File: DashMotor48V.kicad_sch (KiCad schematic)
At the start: 27 parts, among them U1 TPS629203DRLR, U2 TPS629203DRLR, U3 DRV8353SRTAR

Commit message: include the mosfet
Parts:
- added C13: 100nF 50V, dash:CC0603JRX7R9BB104, symbol dash:CC0603JRX7R9BB104
- added C14: GRM155R60J475ME87D, dash:GRM155R60J475ME87D, symbol dash:GRM155R60J475ME87D
- added C15, C16, C17, C18, C19, C20, C21, C22, C23, C24, C25, C26, C27, C28, C29, C30: 10uF, dash:GRM32EC72A106KE05L, symbol dash:GRM32EC72A106KE05L
- added FL1: choe, dash:BLM18AG601SN1D, symbol dash:BLM18AG601SN1D
- added H1, H2, H3: MountingHole_Pad, symbol Mechanical:MountingHole_Pad
- added Q1, Q2, Q3, Q4, Q5, Q6: FDMS039N08B, dash:FDMS039N08B, symbol dash:FDMS039N08B
- added R10: 10K, dash:RT0402DRE0710KL, symbol dash:RT0402DRE0710KL
- added R11, R12: WSLF25121L000FEA, dash:WSLF25121L000FEA, symbol dash:WSLF25121L000FEA
- added R9: 150K 1%, dash:RC0402FR_07150KL, symbol dash:RC0402FR_07150KL
- added U4: STM32F446RCT6, dash:STM32F446RCT6, symbol dash:STM32F446RCT6
- added Y1: CSTNE8M00G550000R0, dash:CSTNE8M00G550000R0, symbol dash:CSTNE8M00G550000R0
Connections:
- net +3.3V: now also FL1.1, U4.1 (VBAT), U4.19 (VDD_4), U4.32 (VDD_1), U4.48 (VDD_2), U4.64 (VDD_3)
- net +48V: now also C15.2, C16.2, C17.2, C18.2, C19.2, C20.2, C21.2, C22.2, C23.2, C24.2, C25.2, C26.2, C27.2, C28.2, C29.2, C30.2, Q1.5 (D_1), Q1.6 (D_2), Q1.7 (D_3), Q1.8 (D_4), Q1.9 (D_5), Q3.5 (D_1), Q3.6 (D_2), Q3.7 (D_3), Q3.8 (D_4), Q3.9 (D_5), Q5.5 (D_1), Q5.6 (D_2), Q5.7 (D_3), Q5.8 (D_4), Q5.9 (D_5), R9.1
- net ENABLE: now also U4.44 (PA11)
- net GHA: now also Q1.4 (G)
- net GHB: now also Q3.4 (G)
- net GHC: now also Q5.4 (G)
- net GLA: now also Q2.4 (G)
- net GLC: now also Q6.4 (G)
- net GND: now also C13.2, C14.1, C15.1, C16.1, C17.1, C18.1, C19.1, C20.1, C21.1, C22.1, C23.1, C24.1, C25.1, C26.1, C27.1, C28.1, C29.1, C30.1, Q6.1 (S_1), Q6.2 (S_2), Q6.3 (S_3), R10.1, R11.1, R12.1, U4.12 (VSSA/VREF-), U4.18 (VSS_4), U4.31 (VSS_1), U4.47 (VSS_2), U4.60 (BOOT0), U4.63 (VSS_3), Y1.2
- net I_A: now also U4.8 (PC0)
- net I_B: now also U4.9 (PC1)
- net PHASA: now also H1.1, Q1.1 (S_1), Q1.2 (S_2), Q1.3 (S_3), Q2.5 (D_1), Q2.6 (D_2), Q2.7 (D_3), Q2.8 (D_4), Q2.9 (D_5)
- net PHASB: now also H2.1, Q3.1 (S_1), Q3.2 (S_2), Q3.3 (S_3), Q4.5 (D_1), Q4.6 (D_2), Q4.7 (D_3), Q4.8 (D_4), Q4.9 (D_5)
- net PHASC: now also H3.1, Q5.1 (S_1), Q5.2 (S_2), Q5.3 (S_3), Q6.5 (D_1), Q6.6 (D_2), Q6.7 (D_3), Q6.8 (D_4), Q6.9 (D_5)
- net PWMA: now also U4.43 (PA10)
- net PWMB: now also U4.42 (PA9)
- net PWMC: now also U4.41 (PA8)
- net SPI-NSS-DRV: now also U4.21 (PA5)
- net SPI-SCK: now also U4.22 (PA6)
- new net: U4.5 (PH0-OSC_IN), Y1.1
- new net: U4.6 (PH1-OSC_OUT), Y1.3
- new net: R10.2, R9.2, U4.15 (PA1)
- new net: Q4.1 (S_1), Q4.2 (S_2), Q4.3 (S_3), R12.2
- new net: C14.2, U4.30 (VCAP_1)
- new net: C13.1, FL1.2, U4.13 (VDDA/VREF+)
- new net: Q2.1 (S_1), Q2.2 (S_2), Q2.3 (S_3), R11.2
- new net CAN_RX: U4.59 (PB7), U4.61 (PB8)
- new net CAN_TX: U4.58 (PB6), U4.62 (PB9)
- new net CS: U4.50 (PA15)
- new net GLB0: Q4.4 (G)
- new net INDICATOR: U4.25 (PC5)
- new net MISO: U4.52 (PC11)
- new net MOSI: U4.53 (PC12)
- new net NRST: U4.7 (NRST)
- new net SCK: U4.51 (PC10)
- new net SPI-MISO: U4.23 (PA7)
- new net TCK: U4.49 (PA14)
- new net TMS: U4.46 (PA13)
- new net USART_RX: U4.17 (PA3)
- new net USART_TX: U4.16 (PA2)
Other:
- moved on the sheet: C10, C11, C12, C6, C7, C8, C9, R7, R8, U3

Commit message: get can chip done
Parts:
- added C31, C33, C34, C35, C36, C37, C38: 100nF 50V, dash:CC0603JRX7R9BB104, symbol dash:CC0603JRX7R9BB104
- added C32: 1uF 100V, dash:CL31B105KCHNNNE, symbol dash:CL31B105KCHNNNE
- added D1: Red, dash:LTST_C191KRKT, symbol dash:LTST-C191KRKT
- added D2: Green, dash:LTST-C190KGKT, symbol dash:LTST-C190KGKT
- added R13, R14: 200oh, dash:RC0402JR-07200RL, symbol dash:RC0402JR-07200RL
- added U5: MA732GQ-Z, dash:MA732GQ-Z, symbol dash:MA732GQ-Z
- added U6: MCP2542FD-E/MF, dash:MCP2542FD_E_MF, symbol dash:MCP2542FD-E_MF
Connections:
- net +3.3V: now also C31.2, C32.2, C33.2, C34.2, C35.2, C36.2, C38.1, R13.1, U5.13 (VDD), U6.5 (VIO)
- net +5V: now also C37.1, U6.3 (VDD)
- net CAN_RX: now also U6.4 (RXD)
- net CAN_TX: now also U6.1 (TXD)
- net CS: now also U5.5 (CS)
- net GND: now also C31.1, C32.1, C33.1, C34.1, C35.1, C36.1, C37.2, C38.2, D1.1, D2.C, U5.17 (PAD), U5.8 (GND), U6.2 (VSS), U6.8 (STBY), U6.9 (EPAD)
- net INDICATOR: now also R14.1
- net MISO: now also U5.7 (MISO)
- net MOSI: now also U5.4 (MOSI)
- net SCK: now also U5.12 (SCLK)
- new net: D1.2, R14.2
- new net: D2.A, R13.2
- new net CANH: U6.7 (CANH)
- new net CANL: U6.6 (CANL)

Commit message: finishing the routing
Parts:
- added CN3(OUT)1, CN3(OUT)2: XT30(2+2)PB-M.G.B, dash:XT30(2+2)PB-M.G.B, symbol dash:XT30(2+2)PB-M.G.B
- added J1, J2: SM07B-SRSS-TB_LF__SN_, dash:SM07B-SRSS-TB, symbol dash:SM07B-SRSS-TB_LF__SN_
- C14: value GRM155R60J475ME87D -> 4.7 µF
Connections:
- net GLB0 is gone; now on net GLB: Q4.4 (G)
- net +3.3V: now also J1.1, J2.1
- net +48V: now also CN3(OUT)1.4, CN3(OUT)2.4
- net CANH: now also CN3(OUT)1.1, CN3(OUT)2.1
- net CANL: now also CN3(OUT)1.2, CN3(OUT)2.2
- net GND: now also CN3(OUT)1.3, CN3(OUT)2.3, J1.3, J2.7
- net MISO: now also J2.3
- net MOSI: now also J2.2
- net NRST: now also J1.5
- net SCK: now also J2.4
- net SPA: now also Q2.1 (S_1), Q2.2 (S_2), Q2.3 (S_3), R11.2
- net SPB: now also Q4.1 (S_1), Q4.2 (S_2), Q4.3 (S_3), R12.2
- net SPI-MISO: now also R7.2, U3.27 (SDO), U4.22 (PA6); no longer U4.23 (PA7)
- net SPI-MOSI: now also U4.23 (PA7)
- net SPI-NSS-DRV: now also U4.20 (PA4); no longer U4.21 (PA5)
- net SPI-SCK: now also U4.21 (PA5); no longer U4.22 (PA6)
- net TCK: now also J1.2
- net TMS: now also J1.4
- net USART_RX: now also J1.7
- net USART_TX: now also J1.6
- net AUX_CS: now reaches U4.54 (PD2)
- net AUX_CS: now also J2.5
- no-connect marks 5 -> 43
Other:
- note added: "Auxiliaries"
- note added: "Can"
- note added: "Encoder"
- note added: "Fets & bulk capacitors"
- note added: "Gate Driver"
- note added: "MCU"
- note added: "Power"
- moved on the sheet: C10, C11, C12, C36, C37, C38, C6, C7, C8, C9, R7, R8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

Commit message: finish schematic
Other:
- company: (none) -> DARoS Lab
- title: (none) -> Dash 48V
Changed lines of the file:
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@@
 	(generator_version "9.0")
 	(paper "User" 550 500)
+	(title_block
+		(title "Dash 48V")
+		(date "2025-12-02")
+		(company "DARoS Lab")
+	)
 	(rectangle
 		(start 191.77 19.05)
@@
 	(text "MCU"
 		(exclude_from_sim no)
-		(at 26.67 25.908 0)
+		(at 29.972 25.4 0)
 		(effects
 			(font
@@
 	(text "Auxiliaries"
 		(exclude_from_sim no)
-		(at 377.444 246.126 0)
+		(at 386.334 246.38 0)
 		(effects
 			(font
@@
 	(text "Gate Driver"
 		(exclude_from_sim no)
-		(at 208.026 26.162 0)
+		(at 216.662 25.4 0)
 		(effects
 			(font
@@
 	(text "Can\n"
 		(exclude_from_sim no)
-		(at 199.898 248.412 0)
+		(at 201.422 246.38 0)
 		(effects
 			(font
@@
 	(text "Encoder"
 		(exclude_from_sim no)
-		(at 32.512 246.634 0)
+		(at 38.608 246.38 0)
 		(effects
 			(font
@@
 	(text "Fets & bulk capacitors"
 		(exclude_from_sim no)
-		(at 392.176 26.416 0)
+		(at 409.702 25.4 0)
 		(effects
 			(font
@@
 	(text "Power"
 		(exclude_from_sim no)
-		(at 45.466 384.81 0)
+		(at 50.292 384.81 0)
 		(effects
 			(font

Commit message: start on routing
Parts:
- H1, H2, H3: footprint (none) -> MountingHole:MountingHole_2.2mm_M2_Pad
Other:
- moved on the sheet: C1, C2, C3, C36, C37, C38, C4, C5, CN3(OUT)1, CN3(OUT)2, J1, J2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

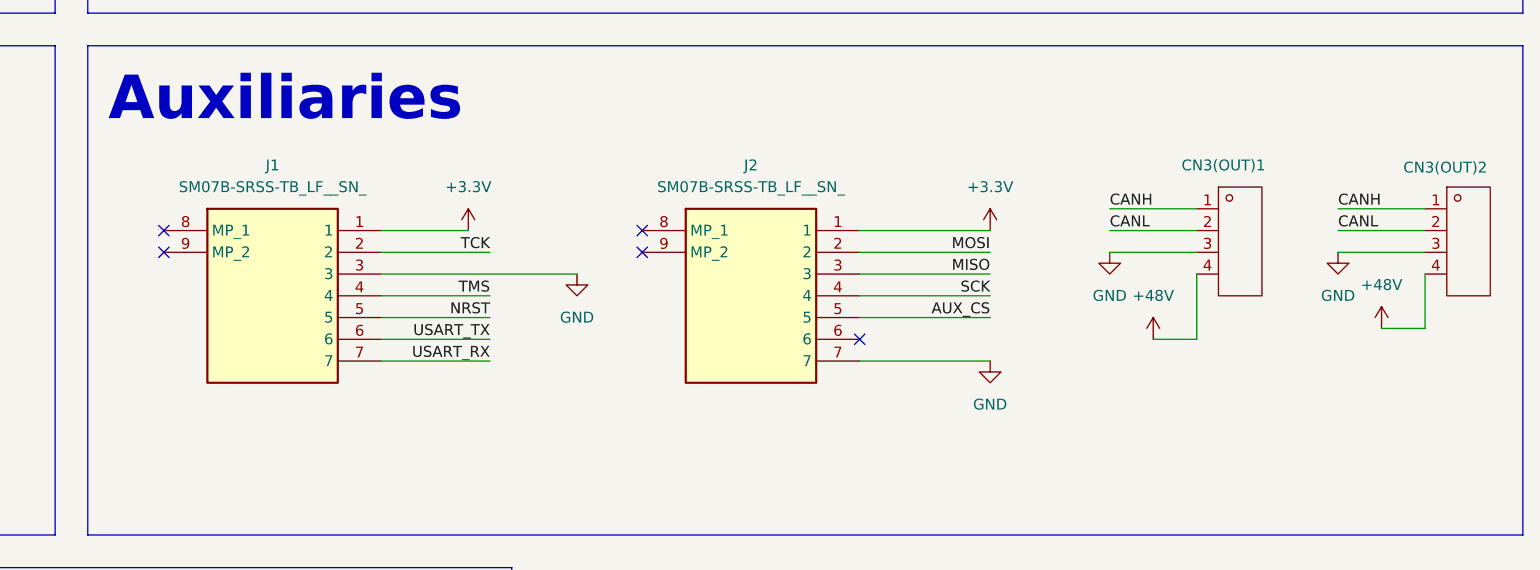
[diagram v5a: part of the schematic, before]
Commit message: get the footprint for the bigger motor
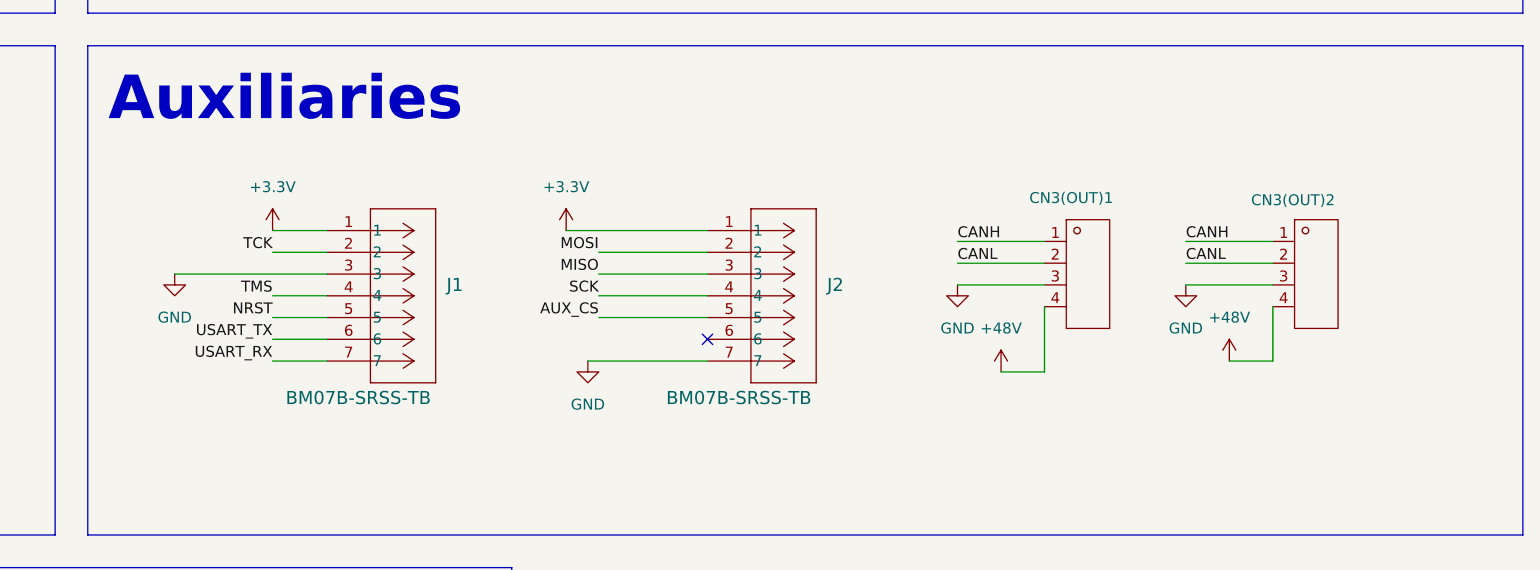
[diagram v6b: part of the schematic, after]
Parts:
- removed J1, J2: SM07B-SRSS-TB_LF__SN_, dash:SM07B-SRSS-TB, symbol dash:SM07B-SRSS-TB_LF__SN_
- added J1, J2: BM07B-SRSS-TB, dash:BM07B-SRSS-TB, symbol dash:BM07B-SRSS-TB
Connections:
- net +3.3V: now also J1.1, J2.1
- net AUX_CS: now also J2.5
- net GND: now also J1.3, J2.7
- net MISO: now also J2.3
- net MOSI: now also J2.2
- net NRST: now also J1.5
- net SCK: now also J2.4
- net TCK: now also J1.2
- net TMS: now also J1.4
- net USART_RX: now also J1.7
- net USART_TX: now also J1.6
- no-connect marks 43 -> 39
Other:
- moved on the sheet: CN3(OUT)1, CN3(OUT)2

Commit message: start placing
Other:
- moved on the sheet: R12

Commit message: 1 draft
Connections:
- net GND: now also VR1.9 (EP)
- net CANH renamed CAN+
- net CANL renamed CAN-
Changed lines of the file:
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@@
 		)
 	)
-	(label "CANH"
+	(label "CAN+"
 		(at 326.39 246.38 180)
 		(effects
@@
 		)
 	)
-	(label "CANL"
+	(label "CAN-"
 		(at 464.82 248.92 0)
 		(effects
@@
 		)
 	)
-	(label "CANH"
+	(label "CAN+"
 		(at 464.82 246.38 0)
 		(effects
@@
 		)
 	)
-	(label "CANL"
+	(label "CAN-"
 		(at 326.39 248.92 180)
 		(effects
@@
 		)
 	)
-	(label "CANL"
+	(label "CAN-"
 		(at 491.49 248.92 0)
 		(effects
@@
 		)
 	)
-	(label "CANH"
+	(label "CAN+"
 		(at 491.49 246.38 0)
 		(effects
@@
 					(unit 1)
 				)
+			)
+		)
+	)
+	(symbol
+		(lib_id "power:GND")
+		(at 80.01 334.01 0)
+		(unit 1)
+		(exclude_from_sim no)
+		(in_bom yes)
+		(on_board yes)
+		(dnp no)
+		(fields_autoplaced yes)
+		(property "Reference" "#PWR072"
+			(at 80.01 340.36 0)
+			(effects
+				(font
+					(size 1.27 1.27)
+				)
+				(hide yes)
+			)
+		)
+		(property "Value" "GND"
+			(at 80.01 339.09 0)
+			(effects
+				(font
+					(size 1.27 1.27)
+				)
+			)
+		)
+		(property "Footprint" ""
+			(at 80.01 334.01 0)
+			(effects
+				(font
+					(size 1.27 1.27)
+				)
+				(hide yes)
+			)
+		)
+		(property "Datasheet" ""
+			(at 80.01 334.01 0)
+			(effects
+				(font
+					(size 1.27 1.27)
+				)
+				(hide yes)
+			)
+		)
+		(property "Description" "Power symbol creates a global label with name \"GND\" , ground"
+			(at 80.01 334.01 0)
+			(effects
+				(font
+					(size 1.27 1.27)
+				)
+				(hide yes)
+			)
+		)
+		(pin "1"
+		)
+		(instances
+			(project "DashMotor48V"
+				(path "/71f0fcc1-c7ad-470c-8d48-d038c53969d3"
+					(reference "#PWR072")
+					(unit 1)
+				)
